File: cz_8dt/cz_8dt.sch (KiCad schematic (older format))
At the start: 547 parts, among them IC1001 74LS09, IC1002 4001, IC1003 4049, IC101 4044, IC102 CD4053B, IC103 HD440072, IC104 4069, IC105 HA11720, IC106 74LS221, IC1101 74LS145, IC1102 74LS145, IC1103 74LS145, IC1104 7406, IC1105 74LS26, IC1106 7408, IC1201 7407, IC1202 7406, IC1203 74LS74, IC301 TA7348P, IC302 TA7348P, IC303 TA7347P, IC304 TA7347P, IC305 TA7348P, IC401 TA7348P, IC402 TA7348P, IC403 TA7347P, IC404 BA7001, IC404 TA7347P, IC601 X0065CE, IC602 74LS221, IC603 74LS221, IC604 74LS221, IC801 TA7608CP, IC901 74159, IC902 74LS126, IC903 74LS126, IC904 74279, IC905 74279, IC906 74279, IC908 74LS11, IC909 7406, Q1001 Q_NPN_BCE, Q1002 Q_NPN_BCE, Q101 Q_NPN_BCE, Q102 Q_NPN_BCE, Q103 Q_NPN_BCE, Q104 Q_NPN_BCE, Q105 Q_NPN_BCE, Q106 Q_NPN_BCE, Q107 Q_NPN_BCE, Q108 Q_NPN_BCE, Q109 Q_NPN_BCE, Q1099 Q_NPN_BCE, Q1101 Q_PNP_BCE, Q1102 Q_NPN_BCE, Q1103 Q_NPN_BCE, Q1104 Q_PNP_BCE, Q1105 Q_NPN_BCE, Q1106 Q_NPN_BCE, Q1107 Q_PNP_BCE, Q1108 Q_NPN_BCE, Q1109 Q_NPN_BCE, Q1110 Q_NPN_BCE, Q1111 Q_NPN_BCE, Q1112 Q_NPN_BCE, Q1113 Q_NPN_BCE, Q1114 Q_NPN_BCE, Q112 Q_NPN_BCE, Q301 Q_NPN_BCE, Q303 Q_NPN_BCE, Q304 Q_NPN_BCE, Q316 Q_NPN_BCE, Q401 Q_NPN_BCE, Q402 Q_PNP_BCE, Q403 Q_NPN_BCE, Q413 Q_NPN_BCE, Q414 Q_NPN_BCE, Q415 Q_NPN_BCE, Q416 Q_NPN_BCE, Q601 Q_NPN_BCE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

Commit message: added more schematics
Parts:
- removed R1177: R, symbol agg-kicad:R
- added C1101, C137, C138: C, symbol agg-kicad:C
- added D104, D301, D302, D927, D928, D929, D930: D, symbol agg-kicad:D
- added G_: CONN_01x13, symbol agg-kicad:CONN_01x13
- added Q1110, Q?: Q_NPN_BCE, symbol Device:Q_NPN_BCE
- added R172, R173, R174, R175, R181, R330, R931, R932 (x2), R933: R, symbol agg-kicad:R
- added R?: 150K, symbol agg-kicad:R
- added R?: 4K7, symbol agg-kicad:R
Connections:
- net labels added: G1, G10, G11, G12, G13, G2, G3, G4, G5, G6, G7, G8, G9, IC401_SEL_1, IC401_SEL_2, J21, K1, K2, M1, M2, M3
- net labels removed: BLUEWIRE
- wire segments 1801 -> 1923
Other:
- note added: "BLUE wire\n"
- note added: "J connector"
- note added: "K-connector"
- note added: "M-connector"
- note added: "R903?\n(duplicate R932)"
- moved on the sheet: C301, C302, C303, C304, C305, C306, C311, C312, C313, C314, C315, C317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

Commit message: added more schematics
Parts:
- added D912, D913, D914: D, symbol agg-kicad:D
- added R930: R, symbol agg-kicad:R
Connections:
- net labels added: J17
- wire segments 1923 -> 2006
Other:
- moved on the sheet: G_, IC902A, IC902B, IC902D, IC908A, IC908B, IC908C

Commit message: more schematics added
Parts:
- added C902: CP, symbol agg-kicad:CP
- added D915, D916, D917, D918, D919, D920, D921, D922, D923, D924, D925, D926, D931, D932, D933, D934, D935: D, symbol agg-kicad:D
- added IC907: 74LS126, symbol 74xx:74LS126
- added R909, R910, R911, R912, R913, R914, R915, R926, R933, R934, R935, R936, R938: R, symbol agg-kicad:R
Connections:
- net labels added: ?V, H1, H10, H11, H12, H2, H3, H4, H5, H6, H7, H8, H9, IC906_2Q_SELECT, J16, J22
- wire segments 2006 -> 2210
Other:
- note added: "check\nfrom\nwhere ?"
- note added: "check\nis H8 coming from this and\nalso from IC903-pin12?"
- note added: "is this going to IC404 (BA7001), \npin 6 that is VCC pin?"
- moved on the sheet: IC902C, IC903A, IC903B, IC903C, IC903D, IC905, IC906, IC909A, IC909E

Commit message: added more schematics
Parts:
- added C101, C107: C, symbol agg-kicad:C
- added Q1115: Q_NPN_BCE, symbol Device:Q_NPN_BCE
- added R111, R113, R117, R1173, R1174, R1179, R1189, R1190, R905, R906, R907, R908, R916, R917, R918, R919, R924, R927: R, symbol agg-kicad:R
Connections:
- net labels added: AUDIO_3_INPUT_L, AUDIO_3_INPUT_R, DSUB_PIN1, DSUB_PIN2, DSUB_PIN3, DSUB_PIN4, DSUB_PIN5, IC901_~S11, J23, N15, N5, N7, N8, VIDEO_3_INPUT
- wire segments 2210 -> 2382
- no-connect marks 32 -> 41
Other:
- note added: "<- Is there conn between here? ->"
- note added: "Check D934 connections"
- note added: "TA304"
- note added: "TP303"
- note added: "TP403"
- note added: "check this again?"
- note added: "check where\n R650 goes?"
- moved on the sheet: C1001, C1002, C1003, C1004, C1005, C103, C104, C109, C110, C1101, C1102, C1104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

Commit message: added more schematics
almoust done with the main board schematics.
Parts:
- removed C1101: C, symbol agg-kicad:C
- removed IC1101, IC1103: 74LS145, symbol 74xx:74LS145
- removed IC304: TA7347P, symbol Switch:TA7347P
- added C1103: C, symbol agg-kicad:C
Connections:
- net labels added: N11
- net labels removed: AUDIO_3_INPUT_L, AUDIO_3_INPUT_R, VIDEO_3_INPUT
- wire segments 2382 -> 2391
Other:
- note added: "TP401"
- note added: "TP402"
- note removed: "<- Is there conn between here? ->"
- note removed: "TA304"
- note removed: "TP303"
- note removed: "check where\n R650 goes?"
- note removed: "is this going to IC404 (BA7001), \npin 6 that is VCC pin?"
- moved on the sheet: C101, C107, IC101, IC102, IC1201F, IC1202F, IC404, IC901, R111, R113, R114, R116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

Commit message: Add files via upload
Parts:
- added Q?: Q_NPN_BCE, symbol Device:Q_NPN_BCE
- added R?: 3K3, symbol agg-kicad:R
- added R?: 560R, symbol agg-kicad:R
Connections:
- net labels removed: BLACK_WIRE, GREENWIRE
- wire segments 2391 -> 2410
- no-connect marks 41 -> 42
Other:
- note added: "TV control Input and output"
- note added: "green wire"
- moved on the sheet: C117, IC101, Q102, R135, R136

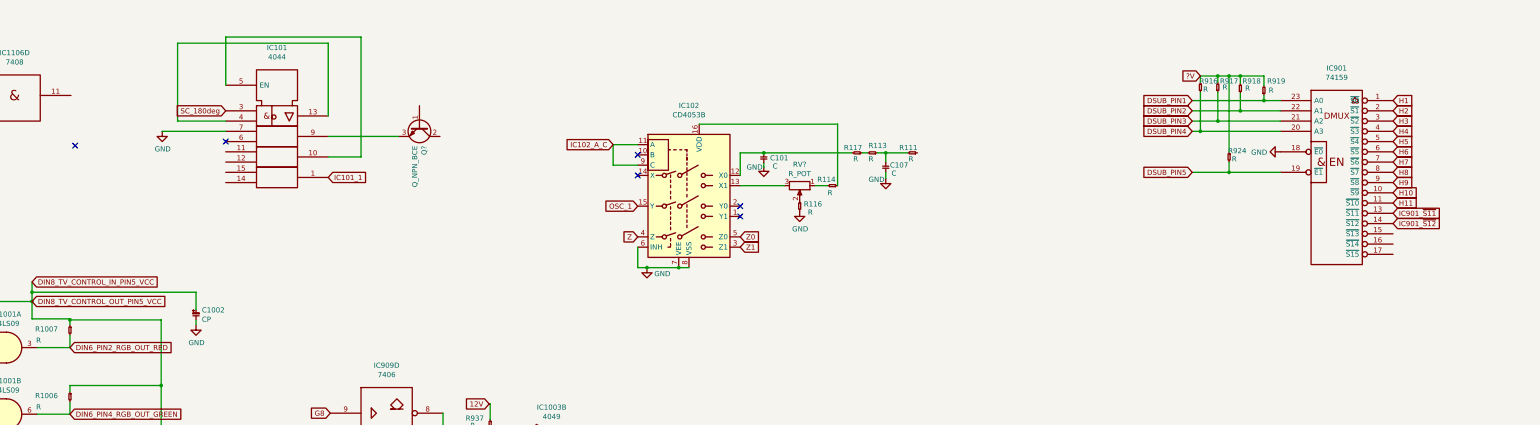
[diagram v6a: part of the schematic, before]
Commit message: added more schematics
now all ICs from mainboard shuold be in the schematics, but some connections are missing. Also resistor values are missing
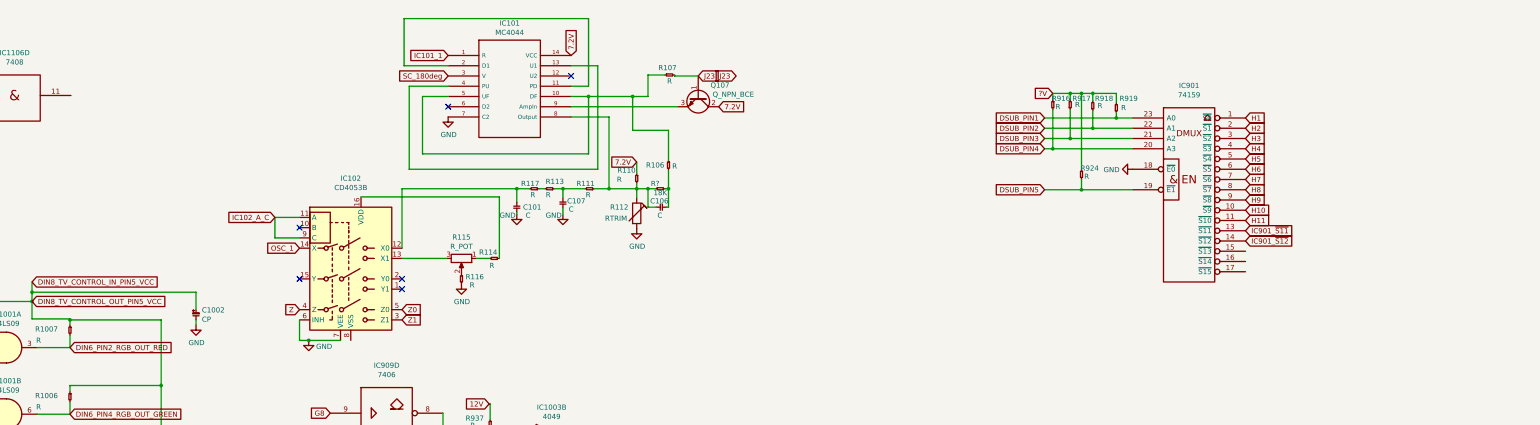
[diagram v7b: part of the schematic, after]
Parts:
- removed IC101: 4044, symbol 4xxx_IEEE:4044
- added C106: C, symbol agg-kicad:C
- added IC101: MC4044, symbol 4xxx_IEEE:MC4044
- added R106, R107, R110: R, symbol agg-kicad:R
- added R112: RTRIM, symbol Device:RTRIM
- added R?: 18K, symbol agg-kicad:R
- gave numbers to parts that had none: 2
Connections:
- wire segments 2410 -> 2440
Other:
- moved on the sheet: C101, C107, IC901, Q107, R111, R113, R114, R115, R116, R117, R916, R917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

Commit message: some missing connection added
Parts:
- added C309, C310, C328: CP, symbol agg-kicad:CP
- added C333: C, symbol agg-kicad:C
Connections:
- net labels added: HA11720_PIN10, HA11720_PIN9, P0_BLUE, P1_RED, P2_GREEN
- net labels removed: P0, P1, P10, P2, P9
- wire segments 2440 -> 2462
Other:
- note added: "BLUE"
- note added: "GREEN"
- note added: "RED"
- note added: "RGB\nin\nBLUE"
- note added: "RGB\nin\nGREEN"
- note added: "RGB\nin\nRED"
- moved on the sheet: C1104, C1105, C1106, Q1112, Q1113, Q1114, R1180, R1181, R1182, R1183, R1184, R1185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
